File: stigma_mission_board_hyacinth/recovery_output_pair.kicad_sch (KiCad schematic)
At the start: 17 parts, among them J10 43045-0400, Q10 TPH4R008NH, Q12 TPH4R008NH, U14 TF0216, U17 TF0216

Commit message: start routing
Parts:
- removed C53, C56: 100n, Capacitor_SMD:C_0603_1608Metric, symbol Device:C
- removed D13, D19: yellow, symbol Device:LED_Small
- removed F1: 10A, Fuse:Fuse_1206_3216Metric, symbol Device:Fuse_Small
- removed J10: 43045-0400, stigma:Molex_Micro-Fit_3.0_43045-0400_2x02_P3.00mm_Horizontal, symbol Connector_Generic:Conn_02x02_Top_Bottom
- removed Q10, Q12: TPH4R008NH, Package_SO:SSOP-8_5.25x5.24mm_P1.27mm, symbol Transistor_FET:DMG2302U
- removed R45, R47: 10k, symbol Device:R_Small
- removed R49, R51: 220, symbol Device:R
- removed R61, R63: 10k, Resistor_SMD:R_0603_1608Metric, symbol Device:R
- removed U14, U17: TF0216, Package_TO_SOT_SMD:SOT-23-5, symbol Driver_FET:ZXGD3003E6
- added C52, C53: 100n, Capacitor_SMD:C_0402_1005Metric, symbol Device:C_Small
- added D16, D17: yellow, LED_SMD:LED_0603_1608Metric, symbol Device:LED_Small
- added F2: 10A, Fuse:Fuse_1206_3216Metric, symbol Device:Fuse_Small
- added JP1: Jumper_3_Open, Connector_PinHeader_2.54mm:PinHeader_1x03_P2.54mm_Vertical, symbol Jumper:Jumper_3_Open
- added Q5, Q6: TPH4R008NH, Package_SO:SSOP-8_5.25x5.24mm_P1.27mm, symbol Transistor_FET:DMG2302U
- added R53, R55, R57, R59: 10k, Resistor_SMD:R_0402_1005Metric, symbol Device:R_Small
- added R54, R56, R58: 220, Resistor_SMD:R_0402_1005Metric, symbol Device:R_Small
- added U15, U16: TF0216, Package_TO_SOT_SMD:SOT-23-5, symbol Driver_FET:ZXGD3003E6
- F3: LCSC (none) -> ---TODO---
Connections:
- net +5V: now also C52.2, C53.2, U15.5 (VCC), U16.5 (VCC)
- net GND: now also C52.1, C53.1, Q5.3 (S), Q6.3 (S), R55.2, R59.2, U15.3 (GND), U16.3 (GND)
- net recovery_high: now also F3.2, F2.2
- net at F3.1: now also JP1.3 (B)
- new net: R58.1, U16.4 (SOURCE)
- new net: Q6.4 (G), R58.2, R59.1
- new net: Q5.4 (G), R54.2, R55.1
- new net: D17.2 (A), R57.2
- new net: R54.1, U15.4 (SOURCE)
- new net: JP1.1 (A), R56.2
- new net: D16.2 (A), R53.2
- new net in1: U15.3 (GND)
- new net in2: R56.1, U16.3 (GND)
- new net out1_high: F2.1, R53.1
- new net out1_low: D16.1 (K), Q5.5 (D)
- new net out2_high: JP1.2 (C), R57.1
- new net out2_low: D17.1 (K), Q6.5 (D)
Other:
- note removed: "Recovery"
- title: Recovery Output -> (none)

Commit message: progress on routing, add some 3d models
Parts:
- JP1: footprint Connector_PinHeader_2.54mm:PinHeader_1x03_P2.54mm_Vertical -> Connector_PinHeader_1.27mm:PinHeader_1x03_P1.27mm_Vertical
- Q5, Q6: footprint Package_SO:SSOP-8_5.25x5.24mm_P1.27mm -> Package_DFN_QFN:DFN-8-1EP_3x3mm_P0.65mm_EP1.55x2.4mm
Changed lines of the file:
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@@
 			)
 		)
-		(property "Footprint" "Package_SO:SSOP-8_5.25x5.24mm_P1.27mm"
+		(property "Footprint" "Package_DFN_QFN:DFN-8-1EP_3x3mm_P0.65mm_EP1.55x2.4mm"
 			(at 88.9 50.165 0)
 			(effects
@@
 			)
 		)
-		(property "Footprint" "Package_SO:SSOP-8_5.25x5.24mm_P1.27mm"
+		(property "Footprint" "Package_DFN_QFN:DFN-8-1EP_3x3mm_P0.65mm_EP1.55x2.4mm"
 			(at 88.9 94.615 0)
 			(effects
@@
 			)
 		)
-		(property "Footprint" "Connector_PinHeader_2.54mm:PinHeader_1x03_P2.54mm_Vertical"
+		(property "Footprint" "Connector_PinHeader_1.27mm:PinHeader_1x03_P1.27mm_Vertical"
 			(at 99.06 68.58 0)
 			(effects

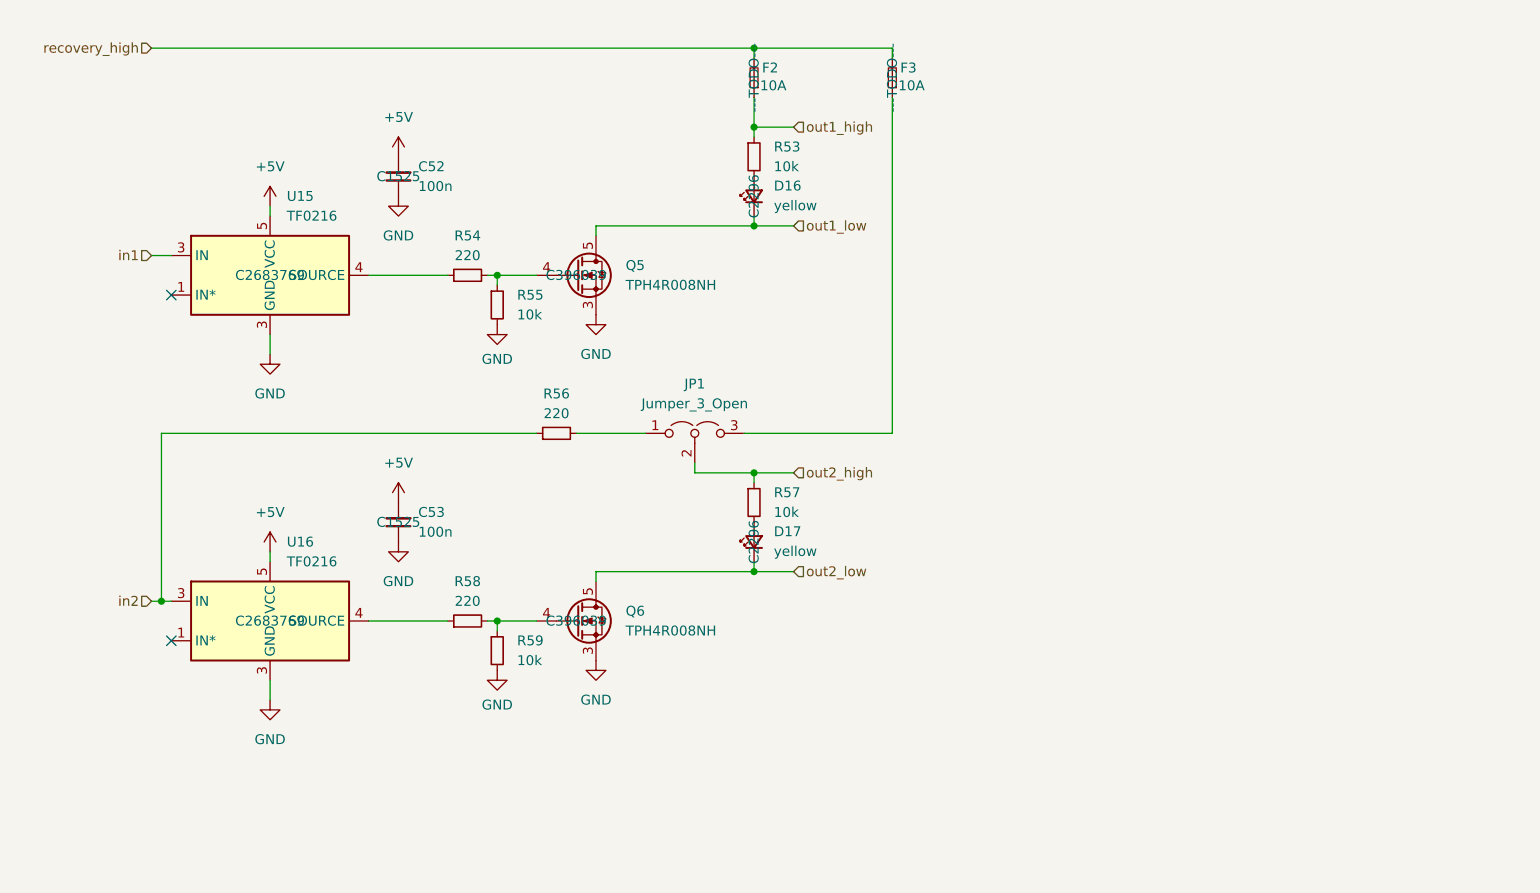
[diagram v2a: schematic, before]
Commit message: progress on mission board layout
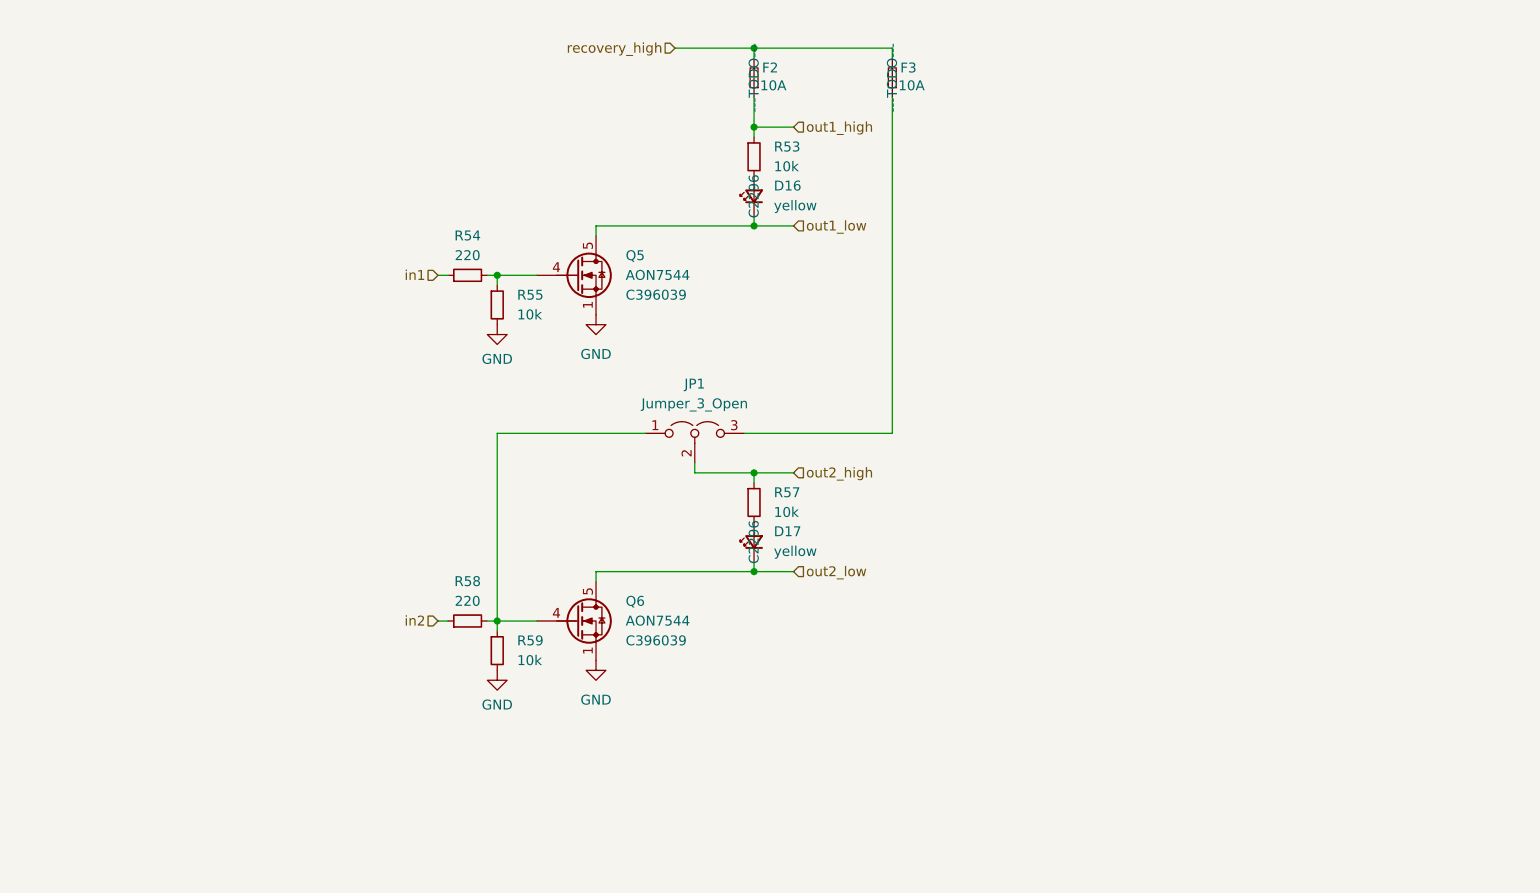
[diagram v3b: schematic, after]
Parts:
- removed C52, C53: 100n, Capacitor_SMD:C_0402_1005Metric, symbol Device:C_Small
- removed R56: 220, Resistor_SMD:R_0402_1005Metric, symbol Device:R_Small
- removed U15, U16: TF0216, Package_TO_SOT_SMD:SOT-23-5, symbol Driver_FET:ZXGD3003E6
- Q5, Q6: value TPH4R008NH -> AON7544; symbol Transistor_FET:DMG2302U -> stigma:AON7544
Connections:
- net GND: now also Q5.1 (S), Q5.2 (S), Q6.1 (S), Q6.2 (S)
- net in1: now also R54.1
- net in2: now also R58.1
- net out1_low: now also Q5.6 (D), Q5.7 (D), Q5.8 (D), Q5.9 (D)
- net out2_low: now also Q6.6 (D), Q6.7 (D), Q6.8 (D), Q6.9 (D)
- net at Q6.4 (G), R58.2, R59.1: now also JP1.1 (A)
- no-connect marks 2 -> 0

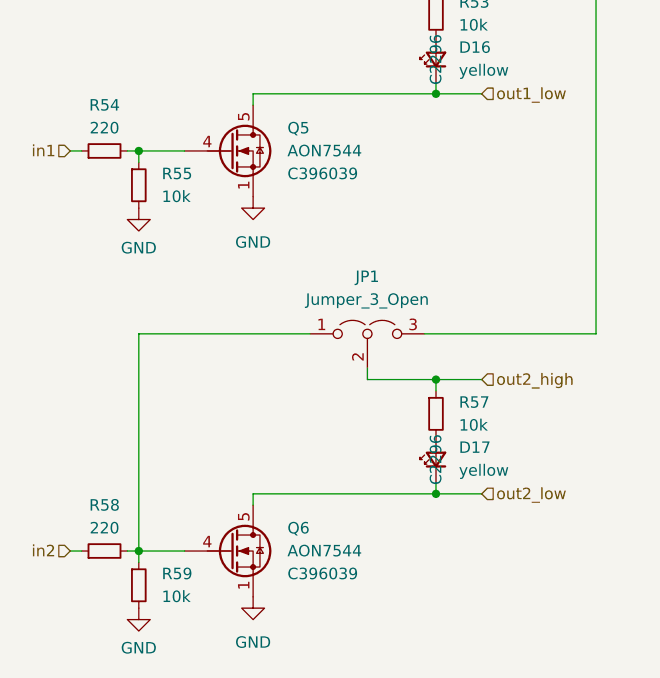
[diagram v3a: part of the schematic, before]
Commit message: Complete routing of mission board
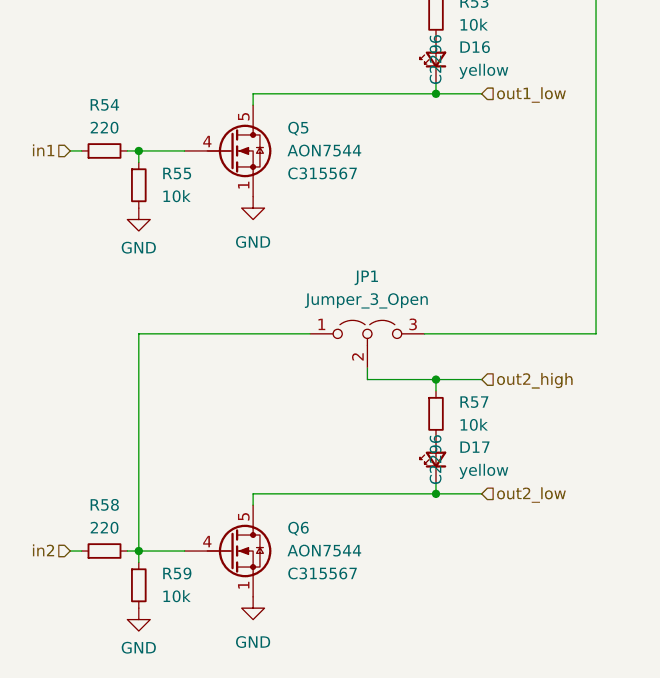
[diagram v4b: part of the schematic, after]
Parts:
- Q5, Q6: LCSC C396039 -> C315567; Manufacturer Toshiba -> (none); Part# DMN2056U-7 -> (none)
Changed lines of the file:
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@@
 			)
 		)
-		(property "Manufacturer" "Toshiba"
+		(property "Manufacturer" ""
 			(at 83.82 48.26 0)
 			(effects
@@
 			)
 		)
-		(property "Part#" "DMN2056U-7"
+		(property "Part#" ""
 			(at 83.82 48.26 0)
 			(effects
@@
 			)
 		)
-		(property "LCSC" "C396039"
+		(property "LCSC" "C315567"
 			(at 90.17 50.7999 0)
 			(effects
@@
 			)
 		)
-		(property "Manufacturer" "Toshiba"
-			(at 83.82 92.71 0)
-			(effects
-				(font
-					(size 1.27 1.27)
-				)
-				(hide yes)
-			)
-		)
-		(property "Part#" "DMN2056U-7"
-			(at 83.82 92.71 0)
-			(effects
-				(font
-					(size 1.27 1.27)
-				)
-				(hide yes)
-			)
-		)
-		(property "LCSC" "C396039"
+		(property "Manufacturer" ""
+			(at 83.82 92.71 0)
+			(effects
+				(font
+					(size 1.27 1.27)
+				)
+				(hide yes)
+			)
+		)
+		(property "Part#" ""
+			(at 83.82 92.71 0)
+			(effects
+				(font
+					(size 1.27 1.27)
+				)
+				(hide yes)
+			)
+		)
+		(property "LCSC" "C315567"
 			(at 90.17 95.2499 0)
 			(effects

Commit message: Last minute changes to mission board
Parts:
- D16, D17: LCSC C2296 -> C2290
- F2, F3: LCSC ---TODO--- -> C207003
- R53, R55, R57, R59: LCSC (none) -> C25744
- R54, R58: value 220 -> 120; LCSC (none) -> C25079
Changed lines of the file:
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@@
 			)
 		)
-		(property "LCSC" "---TODO---"
+		(property "LCSC" "C207003"
 			(at 124.46 22.86 0)
 			(effects
@@
 			)
 		)
-		(property "Value" "220"
+		(property "Value" "120"
 			(at 69.85 90.17 90)
 			(effects
@@
 			)
 		)
+		(property "LCSC" "C25079"
+			(at 69.85 92.71 0)
+			(effects
+				(font
+					(size 1.27 1.27)
+				)
+			)
+		)
 		(pin "2"
 		)
@@
 				)
 				(hide yes)
+			)
+		)
+		(property "LCSC" "C25744"
+			(at 73.66 52.07 0)
+			(effects
+				(font
+					(size 1.27 1.27)
+				)
 			)
 		)
@@
 			)
 		)
-		(property "LCSC" "---TODO---"
+		(property "LCSC" "C207003"
 			(at 106.68 22.86 0)
 			(effects
@@
 			)
 		)
+		(property "LCSC" "C25744"
+			(at 106.68 77.47 0)
+			(effects
+				(font
+					(size 1.27 1.27)
+				)
+			)
+		)
 		(pin "2"
 		)
@@
 			)
 		)
+		(property "LCSC" "C25744"
+			(at 73.66 96.52 0)
+			(effects
+				(font
+					(size 1.27 1.27)
+				)
+			)
+		)
 		(pin "2"
 		)
@@
 			)
 		)
-		(property "Value" "220"
+		(property "Value" "120"
 			(at 69.85 45.72 90)
 			(effects
@@
 			)
 		)
+		(property "LCSC" "C25079"
+			(at 69.85 48.26 0)
+			(effects
+				(font
+					(size 1.27 1.27)
+				)
+			)
+		)
 		(pin "2"
 		)
@@
 			)
 		)
+		(property "LCSC" "C25744"
+			(at 106.68 33.02 0)
+			(effects
+				(font
+					(size 1.27 1.27)
+				)
+			)
+		)
 		(pin "2"
 		)
@@
 			)
 		)
-		(property "LCSC" "C2296"
+		(property "LCSC" "C2290"
 			(at 106.68 38.1 0)
 			(effects
@@
 			)
 		)
-		(property "LCSC" "C2296"
+		(property "LCSC" "C2290"
 			(at 106.68 82.55 0)
 			(effects

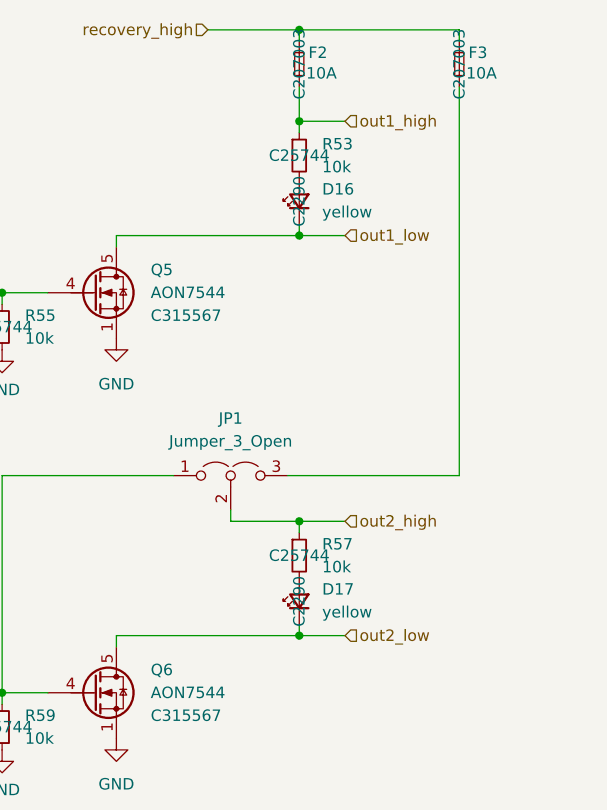
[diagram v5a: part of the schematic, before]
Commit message: replace voltage regulator and increase edge-cut corner radius to match the core board
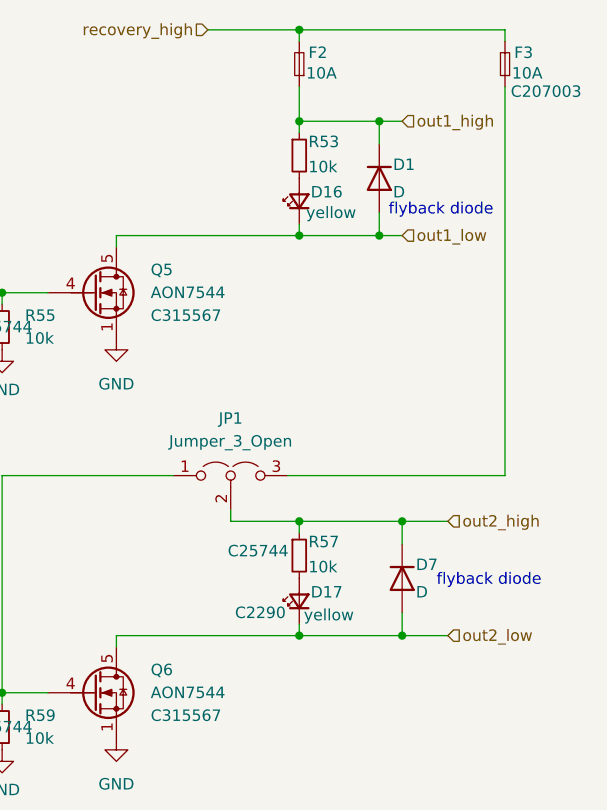
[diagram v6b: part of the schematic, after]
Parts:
- added D1, D7: D, symbol Device:D
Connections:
- net out1_high: now also D1.1 (K)
- net out1_low: now also D1.2 (A)
- net out2_high: now also D7.1 (K)
- net out2_low: now also D7.2 (A)
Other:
- note added: "flyback diode"
- moved on the sheet: F3

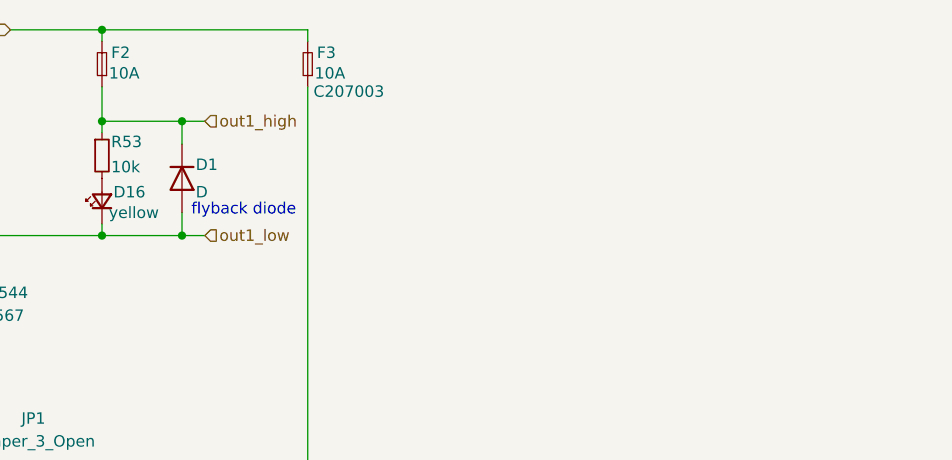
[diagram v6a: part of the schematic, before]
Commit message: fix voltage regulator
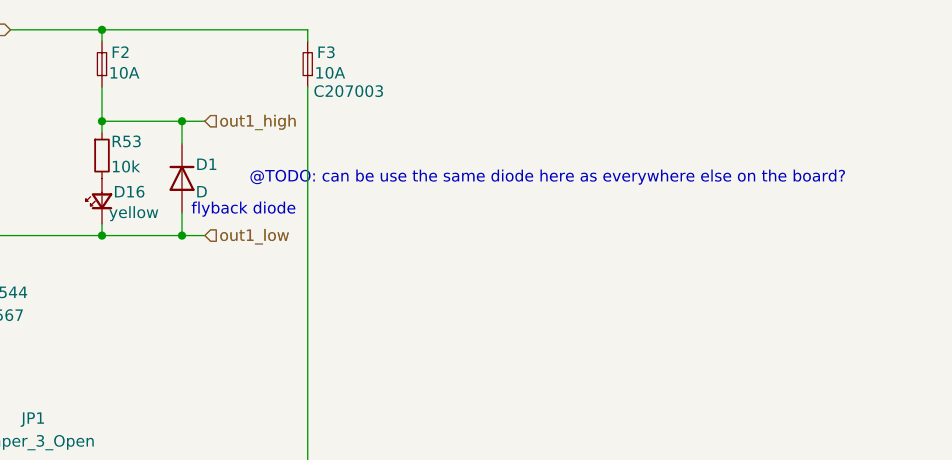
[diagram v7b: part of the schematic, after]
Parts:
- D1: footprint (none) -> Diode_SMD:D_SMA; LCSC# (none) -> C8678
- D7: footprint (none) -> Diode_SMD:D_SMA; LCSC # (none) -> C8678
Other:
- note added: "@TODO: can be use the same diode here as everywhere else on the board?"
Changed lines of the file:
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@@
+		)
+	)
+	(text "@TODO: can be use the same diode here as everywhere else on the board?"
+		(exclude_from_sim no)
+		(at 156.21 35.56 0)
+		(effects
+			(font
+				(size 1.27 1.27)
+			)
 		)
 	)
@@
 			)
 		)
-		(property "Footprint" ""
+		(property "Footprint" "Diode_SMD:D_SMA"
 			(at 118.11 80.01 0)
 			(effects
@@
 		(property "Sim.Pins" "1=K 2=A"
 			(at 118.11 80.01 0)
+			(effects
+				(font
+					(size 1.27 1.27)
+				)
+				(hide yes)
+			)
+		)
+		(property "LCSC #" "C8678"
+			(at 118.11 80.01 90)
 			(effects
 				(font
@@
 			)
 		)
-		(property "Footprint" ""
+		(property "Footprint" "Diode_SMD:D_SMA"
 			(at 115.57 35.56 0)
 			(effects
@@
 			(effects
 				(font
+					(size 1.27 1.27)
+				)
+				(hide yes)
+			)
+		)
+		(property "LCSC#" "C8678"
+			(at 115.57 35.56 90)
+			(effects
+				(font

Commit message: final adjustments for mission board rev2
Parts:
- removed D1, D7: D, Diode_SMD:D_SMA, symbol Device:D
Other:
- note removed: "@TODO: can be use the same diode here as everywhere else on the board?"
- note removed: "flyback diode"
